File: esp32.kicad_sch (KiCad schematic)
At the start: 65 parts, among them J1 USB_C_UART, J10 SPI_1, J11 SPI_2, J12 A1, J13 A0, J14 A2, J15 D0, J16 D1, J17 Conn_01x02, J18 Conn_01x02, J2 USB_C, J3 I2C_0, J4 I2C_1, J5 I2C_2, J6 UART_0, J7 UART_1, J8 UART_2, J9 SPI_0, Q1 S8050, Q2 S8050, SW1 SW_BOOT, SW2 SW_RST, U1 CH340C, U2 ESP32-S3-WROOM-1, U3 XC6220B331MR

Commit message: transopts
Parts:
- removed C17: 100n, Capacitor_SMD:C_0805_2012Metric_Pad1.18x1.45mm_HandSolder, symbol Device:C
- removed J15: D0, Connector:NS-Tech_Grove_1x04_P2mm_Vertical, symbol Connector_Generic:Conn_01x04
- removed J16: D1, Connector:NS-Tech_Grove_1x04_P2mm_Vertical, symbol Connector_Generic:Conn_01x04
- removed R3: 10k, Resistor_SMD:R_0805_2012Metric_Pad1.20x1.40mm_HandSolder, symbol Device:R
- removed U3: XC6220B331MR, Package_TO_SOT_SMD:SOT-23-5, symbol Regulator_Linear:XC6220B331MR
- added C26, C7: 100n, Capacitor_SMD:C_0805_2012Metric_Pad1.18x1.45mm_HandSolder, symbol Device:C
- added D3: 1N5820, symbol Device:D_Schottky
- added J15: EXT_CONN, TerminalBlock:TerminalBlock_MaiXu_MX126-5.0-02P_1x02_P5.00mm, symbol Connector_Generic:Conn_01x02
- added J19, J20: A1, Connector:NS-Tech_Grove_1x04_P2mm_Vertical, symbol Connector_Generic:Conn_01x04
- added L1: L, symbol Device:L
- added R15, R16, R17, R18, R21, R22, R23, R24, R25, R26, R27, R28, R29, R30, R31, R32, R33, R34, R35, R8: 0, symbol Device:R
- added R19, R20, R36, R37, R38, R39: R, symbol Device:R
- added R40, R42, R44, R46: 470, symbol Device:R
- added R41, R43, R45, R47: ~, symbol Device:R
- added U10, U11, U12, U13, U4, U5, U6, U7, U8, U9: Optocoupler_DC_PhotoNPN_AKEC, symbol Isolator:Optocoupler_DC_PhotoNPN_AKEC
- added U14: XL1509-5.0, Package_SO:SOIC-8_3.9x4.9mm_P1.27mm, symbol Regulator_Switching:XL1509-5.0
- added U3: AMS1117-3.3, Package_TO_SOT_SMD:SOT-223-3_TabPin2, symbol Regulator_Linear:AMS1117-3.3
- C18: value 100n -> C; footprint Capacitor_SMD:C_0805_2012Metric_Pad1.18x1.45mm_HandSolder -> (none)
- C6: value 100u -> C; footprint Capacitor_THT:C_Radial_D6.3mm_H7.0mm_P2.50mm -> (none)
- J17: value Conn_01x02 -> PWR_CONN
- J18: value Conn_01x02 -> GND_CONN
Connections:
- net +3V3: now also C26.1, C7.1, J19.2 (Pin_2), J20.2 (Pin_2), U3.2 (VO); no longer C18.1
- net A0: now also R15.2, U4.4; no longer J13.4 (Pin_4)
- net A1: now also R16.2, U6.4; no longer J13.3 (Pin_3)
- net A2: now also R23.2, U5.4; no longer J12.4 (Pin_4)
- net A3: now also R24.2, U7.4; no longer J12.3 (Pin_3)
- net A4: now also R27.2, U8.4; no longer J14.4 (Pin_4)
- net A5: now also R28.2, U9.4; no longer J14.3 (Pin_3)
- net D0: now also R31.2, R40.1
- net D1: now also R32.2, R42.1
- net D2: now also R34.2, R44.1
- net D3: now also R35.2, R46.1
- net GND: now also C6.1, J17.1 (Pin_1), J17.2 (Pin_2), C26.2, C7.2, D3.2 (A), J19.1 (Pin_1), J20.1 (Pin_1), U10.3, U11.3, U12.3, U13.3, U14.1 (VIN), U14.4 (~{EN}), U14.5 (GND), U14.6 (GND), U14.7 (GND), U14.8 (GND), U3.1 (GND), U4.3, U5.3, U6.3, U7.3, U8.3, U9.3
- net VCC renamed +5V
- net +5V: now also C18.1, L1.2, U14.3 (FB), U3.3 (VI); no longer C6.1, J17.1 (Pin_1), J17.2 (Pin_2)
- new net: R40.2, U10.1
- new net: J13.4 (Pin_4), R15.1, R18.1
- new net: R36.2, U5.1
- new net: J13.3 (Pin_3), R16.1, R17.1
- new net: R39.2, U9.1
- new net: D3.1 (K), L1.1, U14.2 (OUT)
- new net: R46.2, U13.1
- new net: J19.4 (Pin_4), R30.1, R31.1
- new net: R42.2, U11.1
- new net: R20.2, U6.1
- new net: J14.3 (Pin_3), R25.1, R28.1
- new net: R37.2, U7.1
- new net: R38.2, U8.1
- new net: J20.3 (Pin_3), R35.1, R8.1
- new net: J20.4 (Pin_4), R33.1, R34.1
- new net: R19.2, U4.1
- new net: J12.4 (Pin_4), R22.1, R23.1
- new net: J12.3 (Pin_3), R21.1, R24.1
- new net: J14.4 (Pin_4), R26.1, R27.1
- new net: R44.2, U12.1
- new net: J19.3 (Pin_3), R29.1, R32.1
- new net A0_EXT: R18.2, R19.1
- new net A1_EXT: R17.2, R20.1
- new net A2_EXT: R22.2, R36.1
- new net A3_EXT: R21.2, R37.1
- new net A4_EXT: R26.2, R38.1
- new net A5_EXT: R25.2, R39.1
- new net D0_EXT: R30.2, R41.1, U10.4
- new net D1_EXT: R29.2, R43.1, U11.4
- new net D2_EXT: R33.2, R45.1, U12.4
- new net D3_EXT: R47.1, R8.2, U13.4
- new net EXT_GND: J15.1 (Pin_1), U10.2, U11.2, U12.2, U13.2, U4.2, U5.2, U6.2, U7.2, U8.2, U9.2
- new net VCC_EXT: J15.2 (Pin_2), R41.2, R43.2, R45.2, R47.2
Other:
- note removed: "TODO: Zmienić stabilizator bo chujowy określić złącza 5v / gnd dodać pin irq do SPIs jak dodać możliwość serw?"
- moved on the sheet: C10, C14, C2, C25, C3, C4, C5, C8, D1, D5, J13, J17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

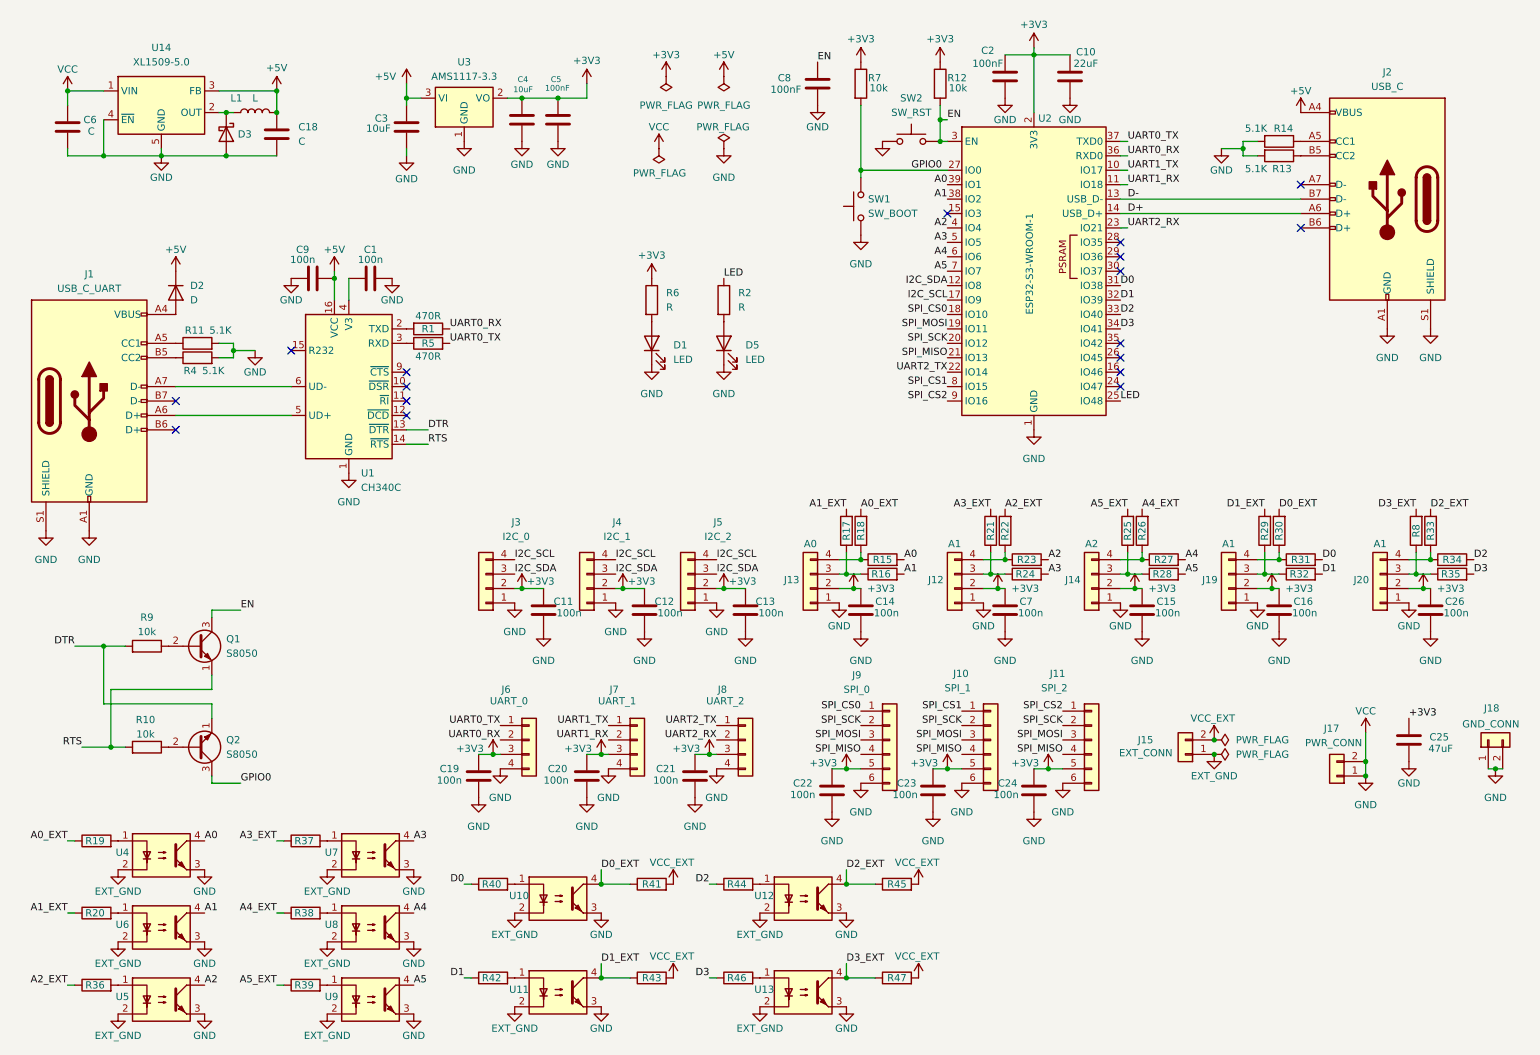
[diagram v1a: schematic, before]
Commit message: change to mosfets and votage divider
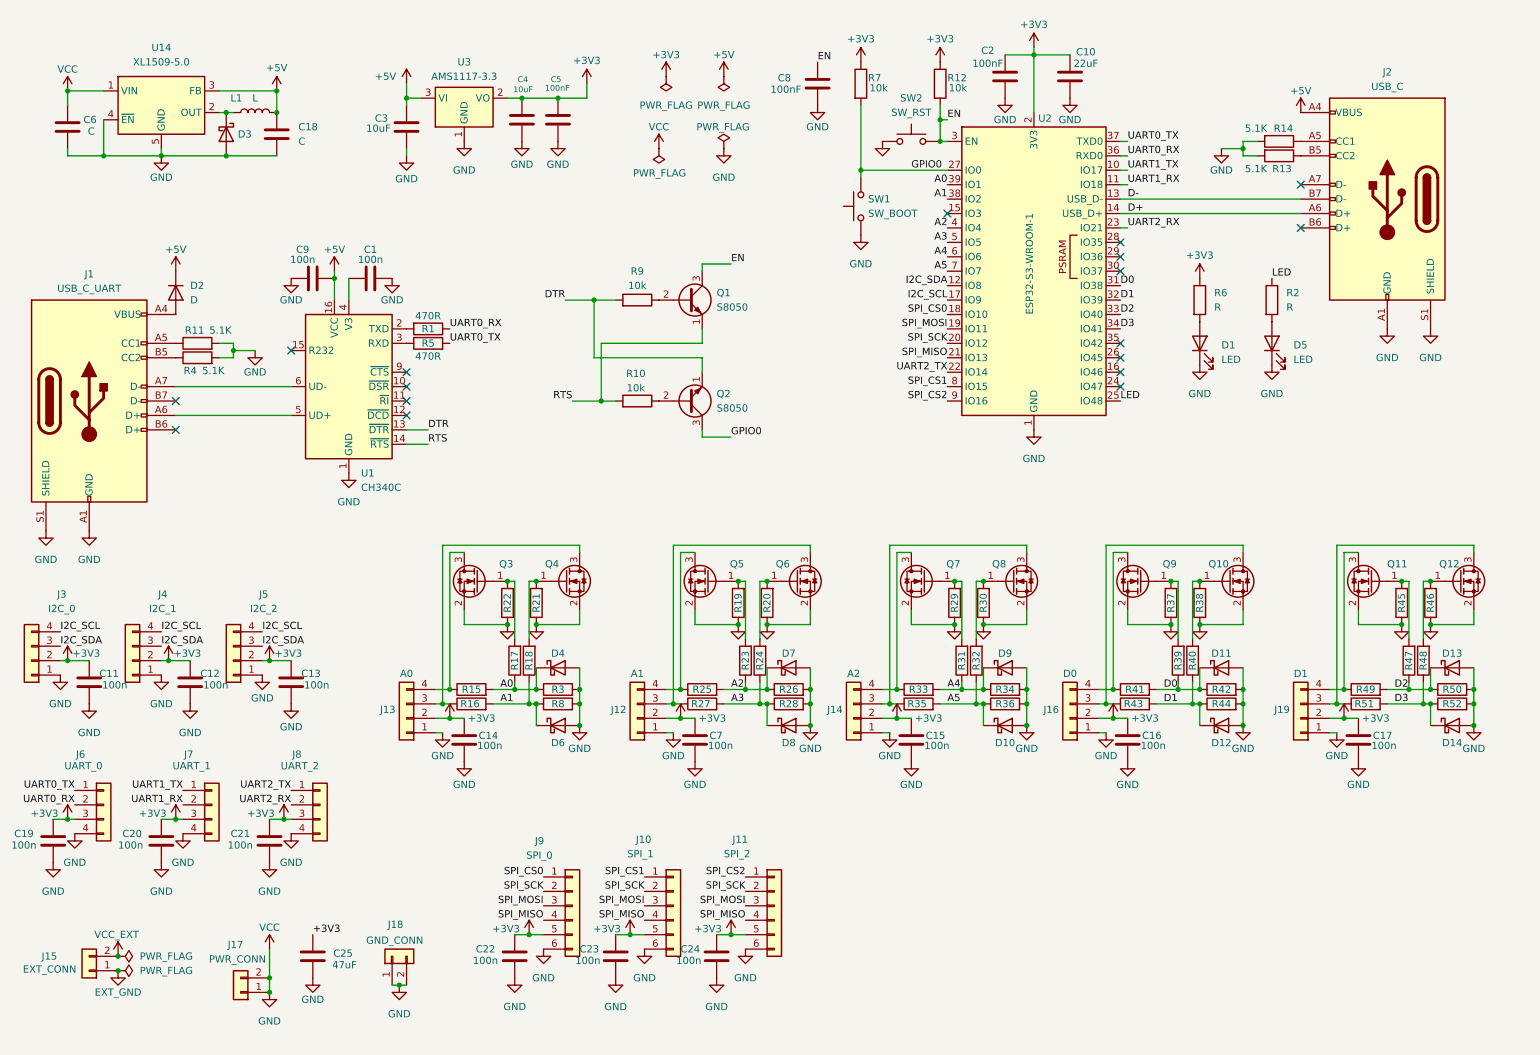
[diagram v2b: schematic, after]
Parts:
- removed C26: 100n, Capacitor_SMD:C_0805_2012Metric_Pad1.18x1.45mm_HandSolder, symbol Device:C
- removed J20: A1, Connector:NS-Tech_Grove_1x04_P2mm_Vertical, symbol Connector_Generic:Conn_01x04
- removed U10, U11, U12, U13, U4, U5, U6, U7, U8, U9: Optocoupler_DC_PhotoNPN_AKEC, symbol Isolator:Optocoupler_DC_PhotoNPN_AKEC
- added C17: 100n, Capacitor_SMD:C_0805_2012Metric_Pad1.18x1.45mm_HandSolder, symbol Device:C
- added D10, D11, D12, D13, D14, D4, D6, D7, D8, D9: D_Schottky, symbol Device:D_Schottky
- added J16: D0, Connector:NS-Tech_Grove_1x04_P2mm_Vertical, symbol Connector_Generic:Conn_01x04
- added Q10, Q11, Q12, Q3, Q4, Q5, Q6, Q7, Q8, Q9: AO3400A, Package_TO_SOT_SMD:SOT-23, symbol Transistor_FET:AO3400A
- added R3, R48, R49, R50, R51, R52: 0, symbol Device:R
- J19: value A1 -> D1
- R19, R20, R36, R37, R38, R39: value R -> 0
- R40, R42, R44, R46: value 470 -> 0
- R41, R43, R45, R47: value ~ -> 0
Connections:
- net A4_EXT is gone; now on net GND: R26.2, R38.1
- net +3V3: now also C17.1, J16.2 (Pin_2)
- net A0: now also R17.1, D4.1 (K), R3.1
- net A1: now also R18.1, R8.1, D6.1 (K)
- net A2: now also R23.1, R25.2, R26.1, D7.1 (K); no longer R23.2
- net A3: now also R24.1, R27.2, R28.1, D8.1 (K); no longer R24.2
- net A4: now also R31.1, R33.2, R34.1, D9.1 (K); no longer R27.2
- net A5: now also R32.1, R35.2, R36.1, D10.1 (K); no longer R28.2
- net D0: now also R39.1, R41.2, R42.1, D11.1 (K); no longer R31.2, R40.1
- net D1: now also R40.1, R43.2, R44.1, D12.1 (K); no longer R32.2, R42.1
- net D2: now also R47.1, D13.1 (K), R49.2, R50.1; no longer R34.2, R44.1
- net D3: now also D14.1 (K), R48.1, R51.2, R52.1; no longer R35.2, R46.1
- net GND: now also R19.1, R20.1, R21.1, R22.1, R28.2, R29.1, R30.1, R34.2, R36.2, R37.1, R42.2, R44.2, R45.1, R46.1, R8.2, C17.2, D10.2 (A), D11.2 (A), D12.2 (A), D13.2 (A), D14.2 (A), D4.2 (A), D6.2 (A), D7.2 (A), D8.2 (A), D9.2 (A), J16.1 (Pin_1), Q10.2 (S), Q11.2 (S), Q12.2 (S), Q3.2 (S), Q4.2 (S), Q5.2 (S), Q6.2 (S), Q7.2 (S), Q8.2 (S), Q9.2 (S), R3.2, R50.2, R52.2
- net VCC_EXT: no longer R41.2, R43.2, R45.2, R47.2
- net at R40.2: now also R38.2, Q10.1 (G)
- net at J13.4 (Pin_4), R15.1: now also Q3.3 (D); no longer R18.1
- net at J13.3 (Pin_3), R16.1: now also Q4.3 (D); no longer R17.1
- net at R39.2: now also R37.2, Q9.1 (G)
- net at R46.2: now also Q12.1 (G), R48.2
- net at R20.2: now also R24.2, Q6.1 (G)
- net at R35.1: now also J14.3 (Pin_3), Q8.3 (D); no longer R8.1
- net at R33.1: now also J14.4 (Pin_4), Q7.3 (D); no longer R34.1
- net at R19.2: now also R23.2, Q5.1 (G)
- net A0_EXT: no longer names the net of R18.2
- net A0_EXT: now also R21.2, Q4.1 (G); no longer R19.1
- net A1_EXT: no longer names the net of R17.2
- net A1_EXT: now also R22.2, Q3.1 (G); no longer R20.1
- removed net A2_EXT: R22.2, R36.1
- removed net A3_EXT: R21.2, R37.1
- removed net A5_EXT: R25.2, R39.1
- net D0_EXT: no longer names the net of R41.1
- net D0_EXT: now also J16.4 (Pin_4), Q9.3 (D); no longer R30.2
- net D1_EXT: no longer names the net of R29.2
- net D1_EXT: now also R31.2, Q7.1 (G); no longer R43.1
- removed net D2_EXT: R33.2, R45.1
- removed net D3_EXT: R47.1, R8.2
- new net: J12.3 (Pin_3), Q6.3 (D), R27.1
- new net: J12.4 (Pin_4), Q5.3 (D), R25.1
- new net: J19.4 (Pin_4), Q11.3 (D), R49.1
- new net: Q11.1 (G), R45.2, R47.2
- new net: J19.3 (Pin_3), Q12.3 (D), R51.1
- new net: Q8.1 (G), R30.2, R32.2
- new net: J16.3 (Pin_3), Q10.3 (D), R43.1
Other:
- moved on the sheet: C11, C12, C13, C14, C19, C20, C21, C22, C23, C24, C25, D1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

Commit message: ldo version
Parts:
- removed C14, C15, C16, C17, C7: 100n, Capacitor_SMD:C_0805_2012Metric_Pad1.18x1.45mm_HandSolder, symbol Device:C
- removed D10, D11, D12, D13, D14, D4, D6, D7, D8, D9: D_Schottky, symbol Device:D_Schottky
- removed J15: EXT_CONN, TerminalBlock:TerminalBlock_MaiXu_MX126-5.0-02P_1x02_P5.00mm, symbol Connector_Generic:Conn_01x02
- removed Q10, Q11, Q12, Q3, Q4, Q5, Q6, Q7, Q8, Q9: AO3400A, Package_TO_SOT_SMD:SOT-23, symbol Transistor_FET:AO3400A
- removed R15, R16, R17, R18, R19, R20, R21, R22, R23, R24, R25, R26, R27, R28, R29, R3, R30, R31, R32, R33, R34, R35, R36, R37, R38, R39, R40, R41, R42, R43, R44, R45, R46, R47, R48, R49, R50, R51, R52, R8: 0, symbol Device:R
- added D5: SS34, Diode_SMD:D_SMA-SMB_Universal_Handsoldering, symbol Device:D_Schottky
- C6: value C -> 470uF; footprint (none) -> Capacitor_SMD:CP_Elec_8x10.5
- C8: renamed from C18; value C -> 180uF; footprint (none) -> Capacitor_SMD:CP_Elec_6.3x5.4
- D1: renamed from D3; value 1N5820 -> SS34; footprint (none) -> Diode_SMD:D_SMB-SMC_Universal_Handsoldering
- J10: renamed from J8; footprint Connector:NS-Tech_Grove_1x04_P2mm_Vertical -> Connector_JST:JST_XH_B4B-XH-A_1x04_P2.50mm_Vertical
- J11: renamed from J3; footprint Connector:NS-Tech_Grove_1x04_P2mm_Vertical -> Connector_JST:JST_XH_B4B-XH-A_1x04_P2.50mm_Vertical
- J12: renamed from J4; footprint Connector:NS-Tech_Grove_1x04_P2mm_Vertical -> Connector_JST:JST_XH_B4B-XH-A_1x04_P2.50mm_Vertical
- J13: renamed from J5; footprint Connector:NS-Tech_Grove_1x04_P2mm_Vertical -> Connector_JST:JST_XH_B4B-XH-A_1x04_P2.50mm_Vertical
- J3: renamed from J13; footprint Connector:NS-Tech_Grove_1x04_P2mm_Vertical -> Connector_JST:JST_XH_B4B-XH-A_1x04_P2.50mm_Vertical
- J4: renamed from J12; footprint Connector:NS-Tech_Grove_1x04_P2mm_Vertical -> Connector_JST:JST_XH_B4B-XH-A_1x04_P2.50mm_Vertical
- J5: renamed from J14; footprint Connector:NS-Tech_Grove_1x04_P2mm_Vertical -> Connector_JST:JST_XH_B4B-XH-A_1x04_P2.50mm_Vertical
- J6: renamed from J16; footprint Connector:NS-Tech_Grove_1x04_P2mm_Vertical -> Connector_JST:JST_XH_B4B-XH-A_1x04_P2.50mm_Vertical
- J7: renamed from J19; footprint Connector:NS-Tech_Grove_1x04_P2mm_Vertical -> Connector_JST:JST_XH_B4B-XH-A_1x04_P2.50mm_Vertical
- J8: renamed from J6; footprint Connector:NS-Tech_Grove_1x04_P2mm_Vertical -> Connector_JST:JST_XH_B4B-XH-A_1x04_P2.50mm_Vertical
- J9: renamed from J7; footprint Connector:NS-Tech_Grove_1x04_P2mm_Vertical -> Connector_JST:JST_XH_B4B-XH-A_1x04_P2.50mm_Vertical
- L1: value L -> 68µH; footprint (none) -> Inductor_SMD:L_6.3x6.3_H3
- Q2: footprint Package_TO_SOT_THT:TO-92_Inline -> Package_TO_SOT_SMD:TSOT-23_HandSoldering
- renumbered C2 to C1, C1 to C10, C19 to C14, C20 to C15, C21 to C16, C25 to C17, C22 to C18, C23 to C19, C10 to C2, C24 to C20, C8 to C3, C3 to C7, D1 to D3, D5 to D4, J2 to J1, J18 to J14, J9 to J15, J10 to J16, J11 to J17, J17 to J18, J1 to J2, R7 to R1, R5 to R10, R4 to R11, R10 to R12, R12 to R2, R14 to R3, R13 to R4, R9 to R5, R2 to R7, R1 to R8, R11 to R9, SW2 to SW1, SW1 to SW2, U3 to U1, U14 to U2, U2 to U3, U1 to U4
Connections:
- net +3V3: no longer J3.2 (Pin_2), J4.2 (Pin_2), J5.2 (Pin_2), J6.2 (Pin_2), J7.2 (Pin_2)
- net DTR: now also Q2.3 (C); no longer Q2.1 (E)
- net GND: no longer C6.1, J18.1 (Pin_1), J18.2 (Pin_2), J3.1 (Pin_1), J4.1 (Pin_1), J5.1 (Pin_1), J6.1 (Pin_1), J7.1 (Pin_1), U2.1 (VIN)
- net GPIO0: now also Q2.1 (E); no longer Q2.3 (C)
- net flex_io2/OUT_1: now reaches J5.3 (Pin_3)
- net flex_io3/OUT_0: now reaches J6.4 (Pin_4)
- net flex_io1/OUT_1: now reaches J4.3 (Pin_3)
- net flex_io1/OUT_0: now reaches J4.4 (Pin_4)
- net flex_io4/OUT_0: now reaches J7.4 (Pin_4)
- net flex_io2/OUT_0: now reaches J5.4 (Pin_4)
- net flex_io0/OUT_1: now reaches J3.3 (Pin_3)
- net flex_io4/OUT_1: now reaches J7.3 (Pin_3)
- net flex_io3/OUT_1: now reaches J6.3 (Pin_3)
- net flex_io0/OUT_0: now reaches J3.4 (Pin_4)
- new net: D5.2 (A), J18.1 (Pin_1), J18.2 (Pin_2)
- new net VCC: C6.1, D5.1 (K), U2.1 (VIN)
- new net flex_io0/+3V3: J3.2 (Pin_2)
- new net flex_io0/GND: J3.1 (Pin_1)
- new net flex_io1/+3V3: J4.2 (Pin_2)
- new net flex_io1/GND: J4.1 (Pin_1)
- new net flex_io2/+3V3: J5.2 (Pin_2)
- new net flex_io2/GND: J5.1 (Pin_1)
- new net flex_io3/+3V3: J6.2 (Pin_2)
- new net flex_io3/GND: J6.1 (Pin_1)
- new net flex_io4/+3V3: J7.2 (Pin_2)
- new net flex_io4/GND: J7.1 (Pin_1)
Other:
- added sheet flex_io0 (flex.kicad_sch)
- added sheet flex_io1 (flex.kicad_sch)
- added sheet flex_io2 (flex.kicad_sch)
- added sheet flex_io3 (flex.kicad_sch)
- added sheet flex_io4 (flex.kicad_sch)
- moved on the sheet: C14, C15, C16, C17, C18, C19, C20, J10, J14, J15, J16, J17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

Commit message: delete unused components
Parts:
- removed C11, C12, C13, C14, C15, C16: 100n, Capacitor_SMD:C_0805_2012Metric_Pad1.18x1.45mm_HandSolder, symbol Device:C
- removed D4: LED, LED_SMD:LED_0805_2012Metric_Pad1.15x1.40mm_HandSolder, symbol Device:LED
- removed J10: UART_2, Connector_JST:JST_XH_B4B-XH-A_1x04_P2.50mm_Vertical, symbol Connector_Generic:Conn_01x04
- removed J11: I2C_0, Connector_JST:JST_XH_B4B-XH-A_1x04_P2.50mm_Vertical, symbol Connector_Generic:Conn_01x04
- removed J12: I2C_1, Connector_JST:JST_XH_B4B-XH-A_1x04_P2.50mm_Vertical, symbol Connector_Generic:Conn_01x04
- removed J13: I2C_2, Connector_JST:JST_XH_B4B-XH-A_1x04_P2.50mm_Vertical, symbol Connector_Generic:Conn_01x04
- removed J18: PWR_CONN, TerminalBlock:TerminalBlock_MaiXu_MX126-5.0-02P_1x02_P5.00mm, symbol Connector_Generic:Conn_01x02
- removed J8: UART_0, Connector_JST:JST_XH_B4B-XH-A_1x04_P2.50mm_Vertical, symbol Connector_Generic:Conn_01x04
- removed J9: UART_1, Connector_JST:JST_XH_B4B-XH-A_1x04_P2.50mm_Vertical, symbol Connector_Generic:Conn_01x04
- removed R7: R, Resistor_SMD:R_0805_2012Metric_Pad1.20x1.40mm_HandSolder, symbol Device:R
- J14: value GND_CONN -> PWR_CONN
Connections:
- net GND: no longer J14.2 (Pin_2)
- net at D5.2 (A): now also J14.2 (Pin_2)
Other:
- moved on the sheet: C17, C18, C19, C20, D5, J14, J15, J16, J17, J3, J4, J5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

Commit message: LMR36520 version
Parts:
- removed C4, C7: 10uF, Capacitor_SMD:C_0805_2012Metric_Pad1.18x1.45mm_HandSolder, symbol Device:C
- removed C5: 100nF, Capacitor_SMD:C_0805_2012Metric_Pad1.18x1.45mm_HandSolder, symbol Device:C
- removed C6: 470uF, Capacitor_SMD:CP_Elec_8x10.5, symbol Device:C
- removed C8: 180uF, Capacitor_SMD:CP_Elec_6.3x5.4, symbol Device:C
- removed D1: SS34, Diode_SMD:D_SMB-SMC_Universal_Handsoldering, symbol Device:D_Schottky
- removed L1: 68µH, Inductor_SMD:L_6.3x6.3_H3, symbol Device:L
- removed U1: AMS1117-3.3, Package_TO_SOT_SMD:SOT-223-3_TabPin2, symbol Regulator_Linear:AMS1117-3.3
- removed U2: XL1509-5.0, Package_SO:SOIC-8_3.9x4.9mm_P1.27mm, symbol Regulator_Switching:XL1509-5.0
